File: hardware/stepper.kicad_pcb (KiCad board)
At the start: 4 copper layers, 40 x 40 mm, 127 parts, among them J101 USB-MINI-B-SMD, J102 DRILL, J103 DRILL, J104 DRILL, J105 DRILL, J401 STACK-UP-HIGH, J402 STACK-DOWN, J403 STACK-UP-HIGH, J404 STACK-DOWN, P201 black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

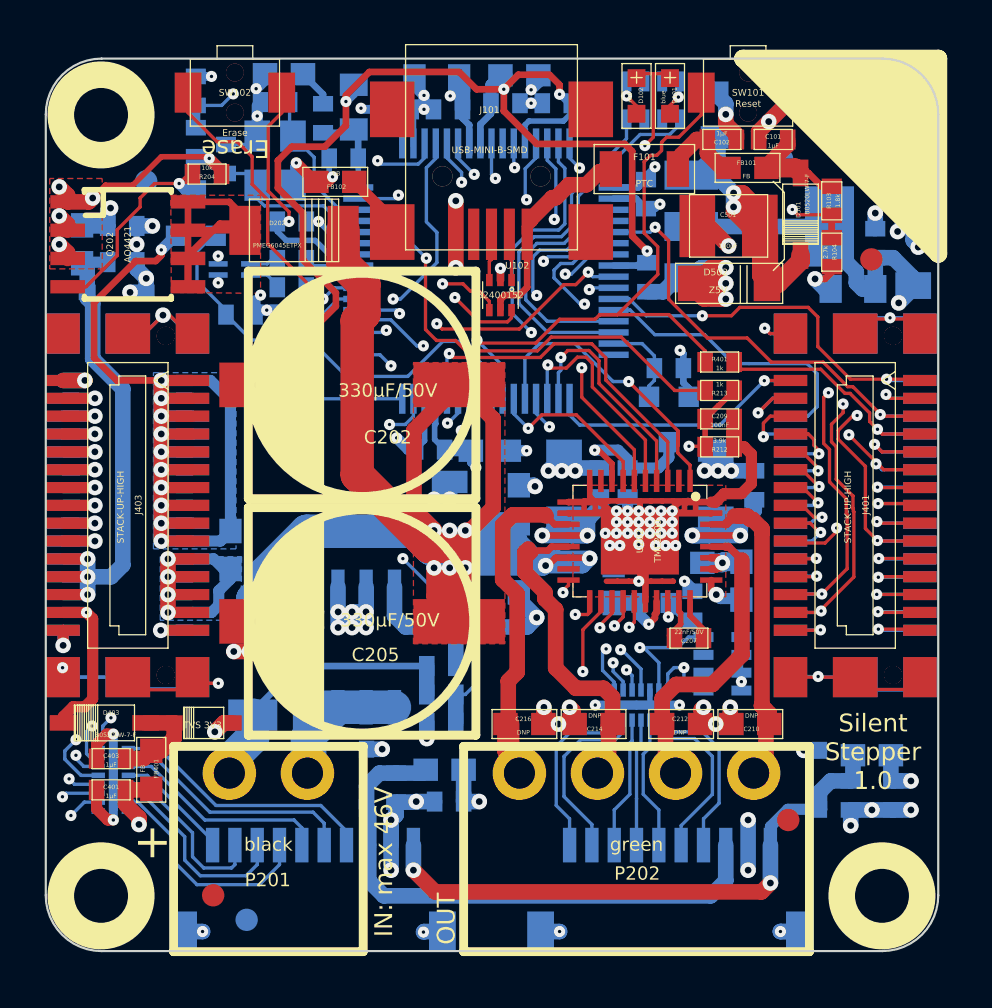
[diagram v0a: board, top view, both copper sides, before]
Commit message: demo stepper mode switching
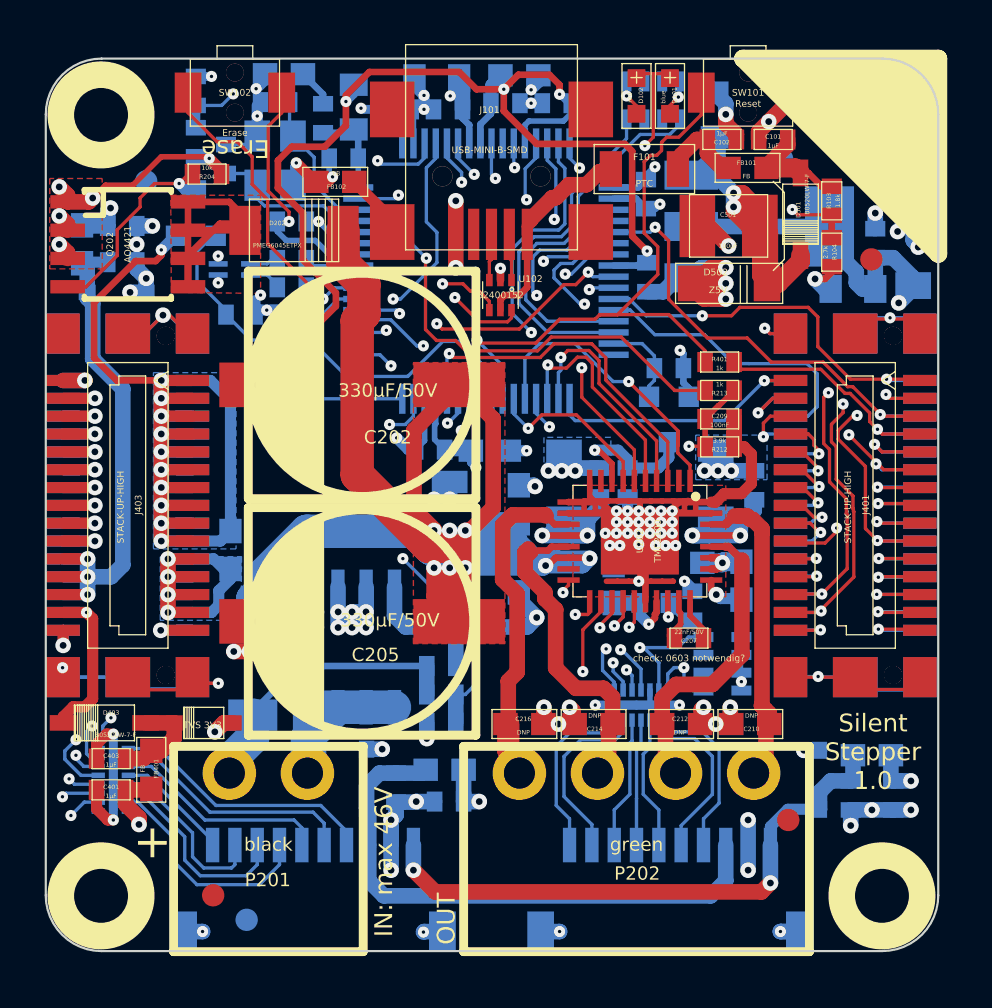
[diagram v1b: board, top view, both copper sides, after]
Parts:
- moved G*** 31.9 mm to (142.8, 91.0)
- moved VAL 0.74 mm to (136.8, 88.8)
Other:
- board text added: "check: 0603 notwendig?"
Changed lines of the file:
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@@
     (links 410)
     (no_connects 2)
-    (area 126.671069 72.726549 166.772591 112.825531)
+    (area 125.845139 71.945139 283.420502 165.440043)
     (thickness 1.6002)
-    (drawings 63)
+    (drawings 64)
     (tracks 2671)
     (zones 0)
@@
   )
   (layers
-    (0 Vorderseite signal)
+    (0 Vorderseite signal hide)
     (1 GND signal hide)
     (2 VCC signal hide)
@@
   )
   (setup
-    (last_trace_width 0.50038)
+    (last_trace_width 0.148)
     (user_trace_width 0.1524)
     (user_trace_width 0.25)
@@
     (aux_axis_origin 126.72568 112.776)
     (grid_origin 166.15 99.35)
-    (visible_elements FFFFDFFF)
+    (visible_elements FFFF5FFF)
     (pcbplotparams
       (layerselection 0x010fc_80000007)
@@
   (module kicad-libraries:SOT563-SPEC (layer Vorderseite)
     (at 147.1 83.375 180)
-    (fp_text reference U102 (at -0.75 1.325 180) (layer F.SilkS)
+    (fp_text reference U102 (at -1.35 0.725 180) (layer F.SilkS)
       (effects (font (size 0.3 0.3) (thickness 0.075)))
     )
@@
   )
   (module kicad-libraries:WEEE_7mm_back (layer Rückseite)
-    (at 136.3 88.35)
+    (at 136.85 88.85)
     (fp_text reference VAL (at 0 0) (layer B.SilkS) hide
-      (effects (font (size 1.143 1.143) (thickness 0.1778)) (justify mirror))
+      (effects (font (size 0.3 0.3) (thickness 0.075)) (justify mirror))
     )
-    (fp_text value WEEE_7mm_back (at 0 0) (layer F.SilkS) hide
-      (effects (font (size 1.143 1.143) (thickness 0.1778)))
+    (fp_text value WEEE_7mm_back (at 0.6 1.6) (layer F.SilkS) hide
+      (effects (font (size 0.3 0.3) (thickness 0.075)))
     )
     (fp_poly (pts (xy 2.5146 -3.56616) (xy 0 -3.56616) (xy -2.51206 -3.56616) (xy -2.51206 0.00254)
@@
   (module kicad-libraries:CE_5mm (layer Rückseite)
     (at 148.4 101.125 180)
-    (fp_text reference VAL (at 0 0 180) (layer B.SilkS) hide
-      (effects (font (size 1.143 1.143) (thickness 0.1778)) (justify mirror))
+    (fp_text reference VAL (at -0.05 0.775 180) (layer B.SilkS) hide
+      (effects (font (size 0.3 0.3) (thickness 0.075)) (justify mirror))
     )
     (fp_text value CE_5mm (at 0 0 180) (layer B.SilkS) hide
-      (effects (font (size 1.143 1.143) (thickness 0.1778)) (justify mirror))
+      (effects (font (size 0.3 0.3) (thickness 0.075)) (justify mirror))
     )
     (fp_poly (pts (xy 2.49936 1.82118) (xy 0.00254 1.81864) (xy -2.49428 1.81864) (xy -2.49428 -0.00254)
@@
   )
   (module kicad-libraries:Logo_31x31 (layer Rückseite)
-    (at 173.55 82.85 180)
+    (at 142.75 91.05 180)
     (fp_text reference G*** (at 1.34874 -2.97434 180) (layer B.SilkS) hide
       (effects (font (size 0.29972 0.29972) (thickness 0.0762)) (justify mirror))
@@
     )
   )
+  (gr_text "check: 0603 notwendig?" (at 155.55 99.65) (layer F.SilkS)
+    (effects (font (size 0.29972 0.29972) (thickness 0.07493)))
+  )
   (gr_text "Silent\nStepper\n1.0" (at 163.8 103.85) (layer F.SilkS)
     (effects (font (size 0.8 0.8) (thickness 0.15)))
   )
-  (gr_text tinkerforge.com (at 174.05 87.25) (layer B.SilkS)
-    (effects (font (size 0.8 0.8) (thickness 0.15)) (justify mirror))
+  (gr_text tinkerforge.com (at 139.65 94.75) (layer B.SilkS)
+    (effects (font (size 0.7 0.7) (thickness 0.15)) (justify mirror))
   )
   (gr_line (start 147.35134 109.17484) (end 147.80092 109.17484) (angle 90) (layer B.SilkS) (width 0.24892))
@@
   (segment (start 160.1019 88.0019) (end 159.3946 88.0019) (width 0.1498) (layer Vorderseite) (net 21))
   (segment (start 150.19904 88.02262) (end 150.19904 88.74904) (width 0.1524) (layer Rückseite) (net 22))
-  (segment (start 156.9385 89.2) (end 158.927 87.2115) (width 0.1524) (layer Rückseite) (net 22))
-  (segment (start 150.65 89.2) (end 156.9385 89.2) (width 0.1524) (layer Rückseite) (net 22))
-  (segment (start 150.19904 88.74904) (end 150.65 89.2) (width 0.1524) (layer Rückseite) (net 22))
+  (segment (start 157.1385 89) (end 158.927 87.2115) (width 0.1524) (layer Rückseite) (net 22))
+  (segment (start 150.45 89) (end 157.1385 89) (width 0.1524) (layer Rückseite) (net 22))
+  (segment (start 150.19904 88.74904) (end 150.45 89) (width 0.1524) (layer Rückseite) (net 22))
   (via (at 158.927 87.2115) (size 0.5) (layers Vorderseite Rückseite) (net 22))
   (segment (start 160.0922 87.2115) (end 158.927 87.2115) (width 0.1498) (layer Rückseite) (net 22))
@@
       )
     )
+  )
+  (zone (net 24) (net_name STACK-PGND) (layer Rückseite) (hatch edge 0.508)
+    (connect_pads yes (clearance 0.15))
+    (min_thickness 0.15)
+    (fill yes (arc_segments 16) (thermal_gap 0.3) (thermal_bridge_width 0.3))
+    (polygon
+      (pts
+        (xy 155.85 89.65) (xy 155.85 91.65) (xy 159.05 91.65) (xy 159.05 89.65)
+      )
+    )
+  )
+  (zone (net 24) (net_name STACK-PGND) (layer Rückseite) (hatch edge 0.508)
+    (connect_pads yes (clearance 0.15))
+    (min_thickness 0.15)
+    (fill yes (arc_segments 16) (thermal_gap 0.3) (thermal_bridge_width 0.3))
+    (polygon
+      (pts
+        (xy 149.05 89.75) (xy 149.05 91.45) (xy 152.05 91.45) (xy 152.05 89.75)
+      )
+    )

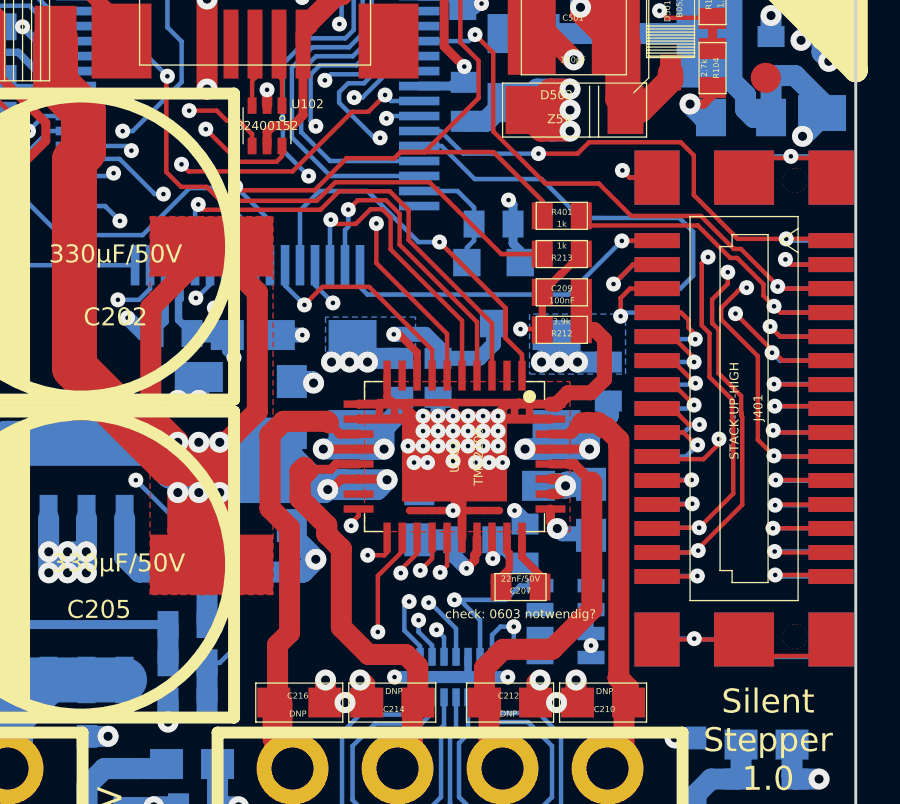
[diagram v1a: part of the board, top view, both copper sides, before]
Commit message: changed to tmc2130
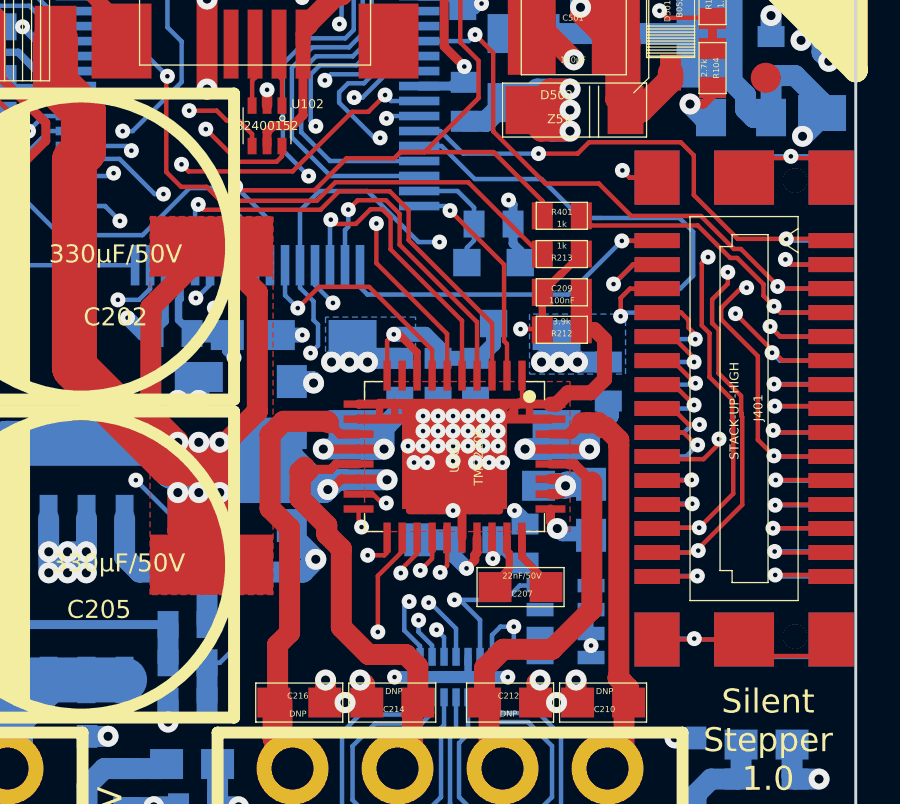
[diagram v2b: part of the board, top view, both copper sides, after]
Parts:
- removed Q1: MOSFET_P, SOT23GDS
- removed R1: 10k, kicad-libraries:0402E
- removed U202: TMC2100, kicad-libraries:QFN36_5X6
- added Q204: MOSFET_P, SOT23GDS, B.Cu at (154.7, 89.0)
- added R209: 10k, kicad-libraries:0402E, B.Cu at (154.7, 86.7)
- added R210: 1k, kicad-libraries:0402E, B.Cu at (154.1, 91.8)
- added U201: TMC2100, kicad-libraries:QFN36_5X6, F.Cu at (153.3, 94.4)
- C207: footprint kicad-libraries:0402E -> kicad-libraries:0603E
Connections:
- FILTER301 pad 8: (no net) -> Net-(FILTER301-Pad8)
- FILTER301 pad 9: (no net) -> Net-(FILTER301-Pad9)
- FILTER302 pad 8: (no net) -> Net-(FILTER302-Pad8)
- FILTER302 pad 9: (no net) -> Net-(FILTER302-Pad9)
- J101 pad 4: (no net) -> Net-(J101-Pad4)
- RP101 pad 2: (no net) -> Net-(RP101-Pad2)
- RP101 pad 3: (no net) -> Net-(RP101-Pad3)
- RP101 pad 6: (no net) -> Net-(RP101-Pad6)
- RP101 pad 7: (no net) -> Net-(RP101-Pad7)
- RP301 pad 6: (no net) -> Net-(RP301-Pad6)
- RP301 pad 7: (no net) -> Net-(RP301-Pad7)
- U101 pad 10: (no net) -> Net-(U101-Pad10)
- U101 pad 32: (no net) -> PWR-CS
- U101 pad 34: PWR-CFG1 -> PWR-SDI
- U101 pad 35: PWR-CFG0 -> PWR-SDO
- U101 pad 37: PWR-CLK -> PWR-DC0
- U101 pad 40: (no net) -> Net-(U101-Pad40)
- U101 pad 44: PWR-CFG2 -> PWR-SCK
- U101 pad 50: (no net) -> Net-(U101-Pad50)
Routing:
- net PWR-DC0: track 0.00 -> 20.2 mm, vias 0 -> 3
- net PWR-CFG2: track 16.3 -> 0.00 mm, vias 1 -> 0
- net PWR-SCK: track 0.00 -> 16.3 mm, vias 0 -> 1
- net PWR-CLK: track 13.7 -> 0.00 mm, vias 1 -> 0
- net PWR-CFG1: track 10.4 -> 0.00 mm, vias 1 -> 0
- net PWR-SDI: track 0.00 -> 10.4 mm, vias 0 -> 1
- net PWR-SDO: track 0.00 -> 10.2 mm, vias 0 -> 1
- net PWR-CFG0: track 10.2 -> 0.00 mm, vias 1 -> 0
- net PWR-CS: track 0.00 -> 7.38 mm, vias 0 -> 1
- net STACK-PGND: track 274.7 -> 278.2 mm
- net VEE: track 97.6 -> 95.4 mm
- net Net-(C201-Pad2): track 6.56 -> 8.03 mm
- net PWR-CFG5: track 25.1 -> 26.1 mm
- net PWR-CFG4: track 27.0 -> 27.8 mm
- net STACK-SER-RXD: track 36.8 -> 37.4 mm
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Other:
- board text removed: "check: 0603 notwendig?"

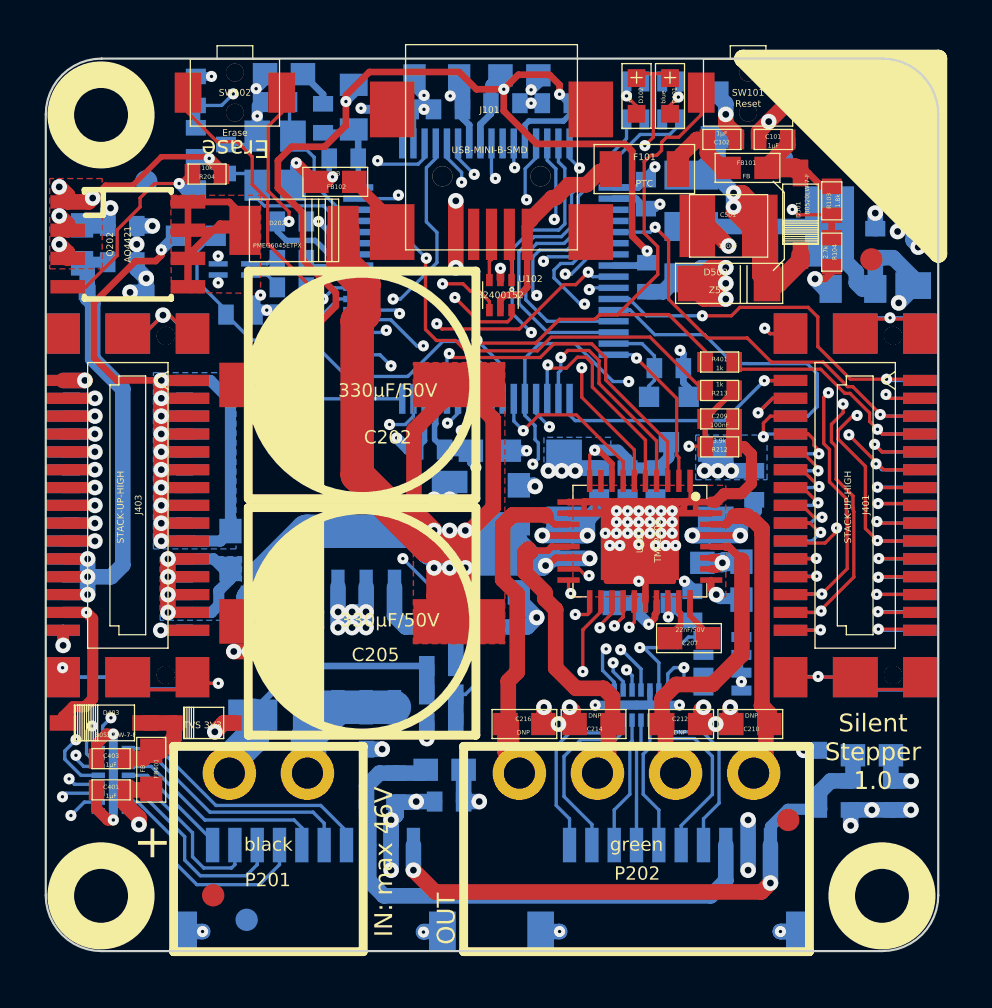
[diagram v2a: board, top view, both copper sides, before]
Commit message: remove unnecessary signals, add external clock
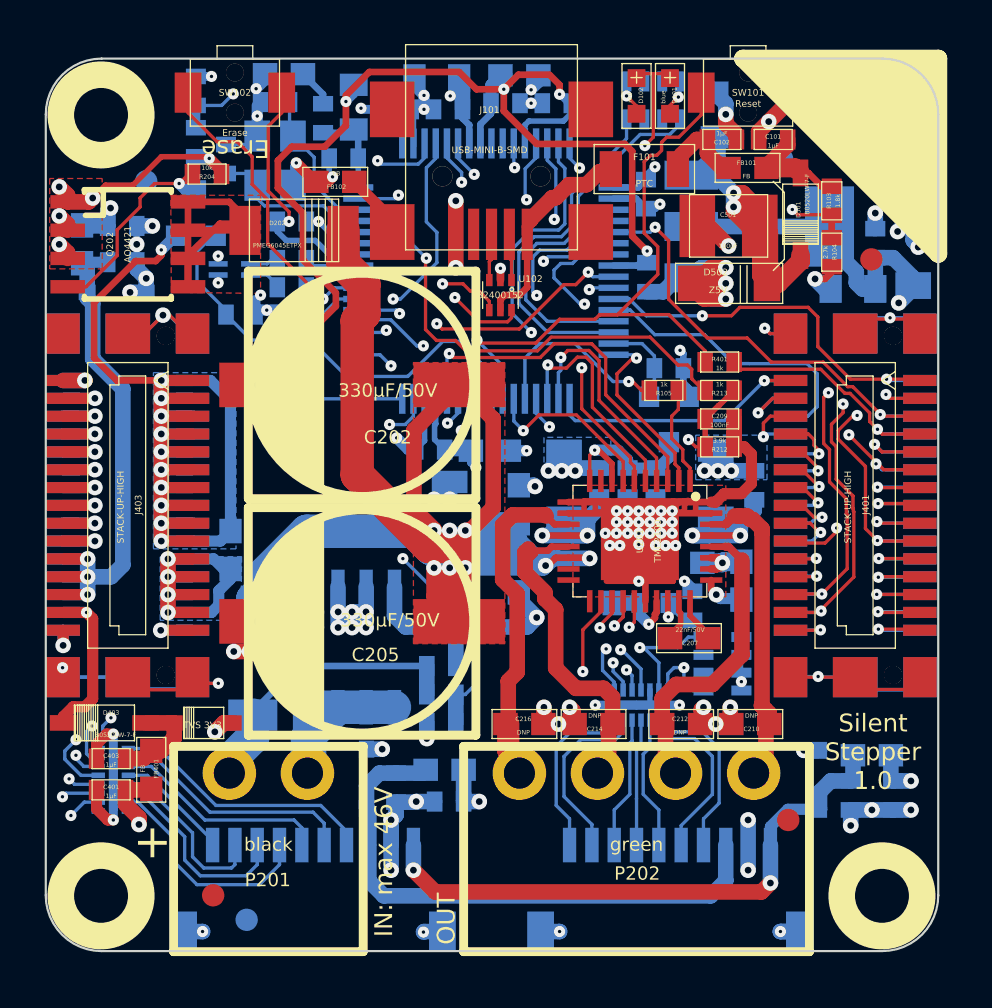
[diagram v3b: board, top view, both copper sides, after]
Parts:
- added R105: 1k, kicad-libraries:0402E, F.Cu at (154.4, 87.7)
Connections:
- FILTER301 pad 8: Net-(FILTER301-Pad8) -> (no net)
- FILTER301 pad 9: Net-(FILTER301-Pad9) -> (no net)
- FILTER302 pad 8: Net-(FILTER302-Pad8) -> (no net)
- FILTER302 pad 9: Net-(FILTER302-Pad9) -> (no net)
- J101 pad 4: Net-(J101-Pad4) -> (no net)
- RP101 pad 2: Net-(RP101-Pad2) -> (no net)
- RP101 pad 3: Net-(RP101-Pad3) -> (no net)
- RP101 pad 6: Net-(RP101-Pad6) -> (no net)
- RP101 pad 7: Net-(RP101-Pad7) -> (no net)
- RP301 pad 6: Net-(RP301-Pad6) -> (no net)
- RP301 pad 7: Net-(RP301-Pad7) -> (no net)
- U101 pad 10: Net-(U101-Pad10) -> (no net)
- U101 pad 23: PWR-CFG5 -> (no net)
- U101 pad 37: PWR-DC0 -> Net-(R105-Pad1)
- U101 pad 40: Net-(U101-Pad40) -> (no net)
- U101 pad 50: Net-(U101-Pad50) -> (no net)
- U101 pad 9: PWR-CFG4 -> (no net)
- U201 pad 1: STACK-PGND -> PWR-CLK
- U201 pad 17: PWR-DC0 -> (no net)
- U201 pad 18: PWR-CFG4 -> (no net)
- U201 pad 19: PWR-CFG5 -> (no net)
- U201 pad 9: Net-(U201-Pad9) -> (no net)
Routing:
- net PWR-CFG4: track 27.8 -> 0.00 mm, vias 2 -> 0
- net PWR-CFG5: track 26.1 -> 0.00 mm, vias 2 -> 0
- net PWR-DC0: track 20.2 -> 0.00 mm, vias 3 -> 0
- net Net-(R105-Pad1): track 0.00 -> 8.54 mm, vias 0 -> 1
- net PWR-CLK: track 0.00 -> 4.52 mm
- net STACK-PGND: track 278.2 -> 274.7 mm
- net PWR-CS: track 7.38 -> 8.21 mm

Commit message: change driver type to tmc2130
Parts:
- removed Q204: MOSFET_P, SOT23GDS
- C207: value 22nF/50V -> 22nF/50V-low
- R209: value 10k -> 0; footprint kicad-libraries:0402E -> kicad-libraries:0603E
- U201: value TMC2100 -> TMC2130
- moved R209 2.35 mm to (154.6, 89.0), turned to 270 degrees
- moved U102 0.12 mm to (147.1, 83.5)
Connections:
- R209 pad 2: 3V3 -> Net-(C201-Pad2)
- U101 pad 37: Net-(R105-Pad1) -> (no net)
- U101 pad 9: (no net) -> Net-(R105-Pad1)
- U201 pad 18: (no net) -> STACK-PGND
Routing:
- net Net-(R105-Pad1): track 8.54 -> 15.7 mm, vias 1 -> 2
- net STACK-PGND: track 274.7 -> 278.6 mm
- net 3V3: track 182.2 -> 179.4 mm, vias 13 -> 12
- net STACK-RESET: track 28.4 -> 26.3 mm
- net GND: track 429.5 -> 427.5 mm
- net PWR-STEP: track 15.6 -> 14.2 mm
- net STACK-SPI-MOSI: track 23.7 -> 22.4 mm
- net Net-(L101-Pad3): track 15.2 -> 16.2 mm
- net BRICKLET-IO1_3: track 33.8 -> 33.1 mm
